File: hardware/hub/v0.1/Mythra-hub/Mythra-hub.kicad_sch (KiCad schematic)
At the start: 1 part, among them U1 TUSB8042A

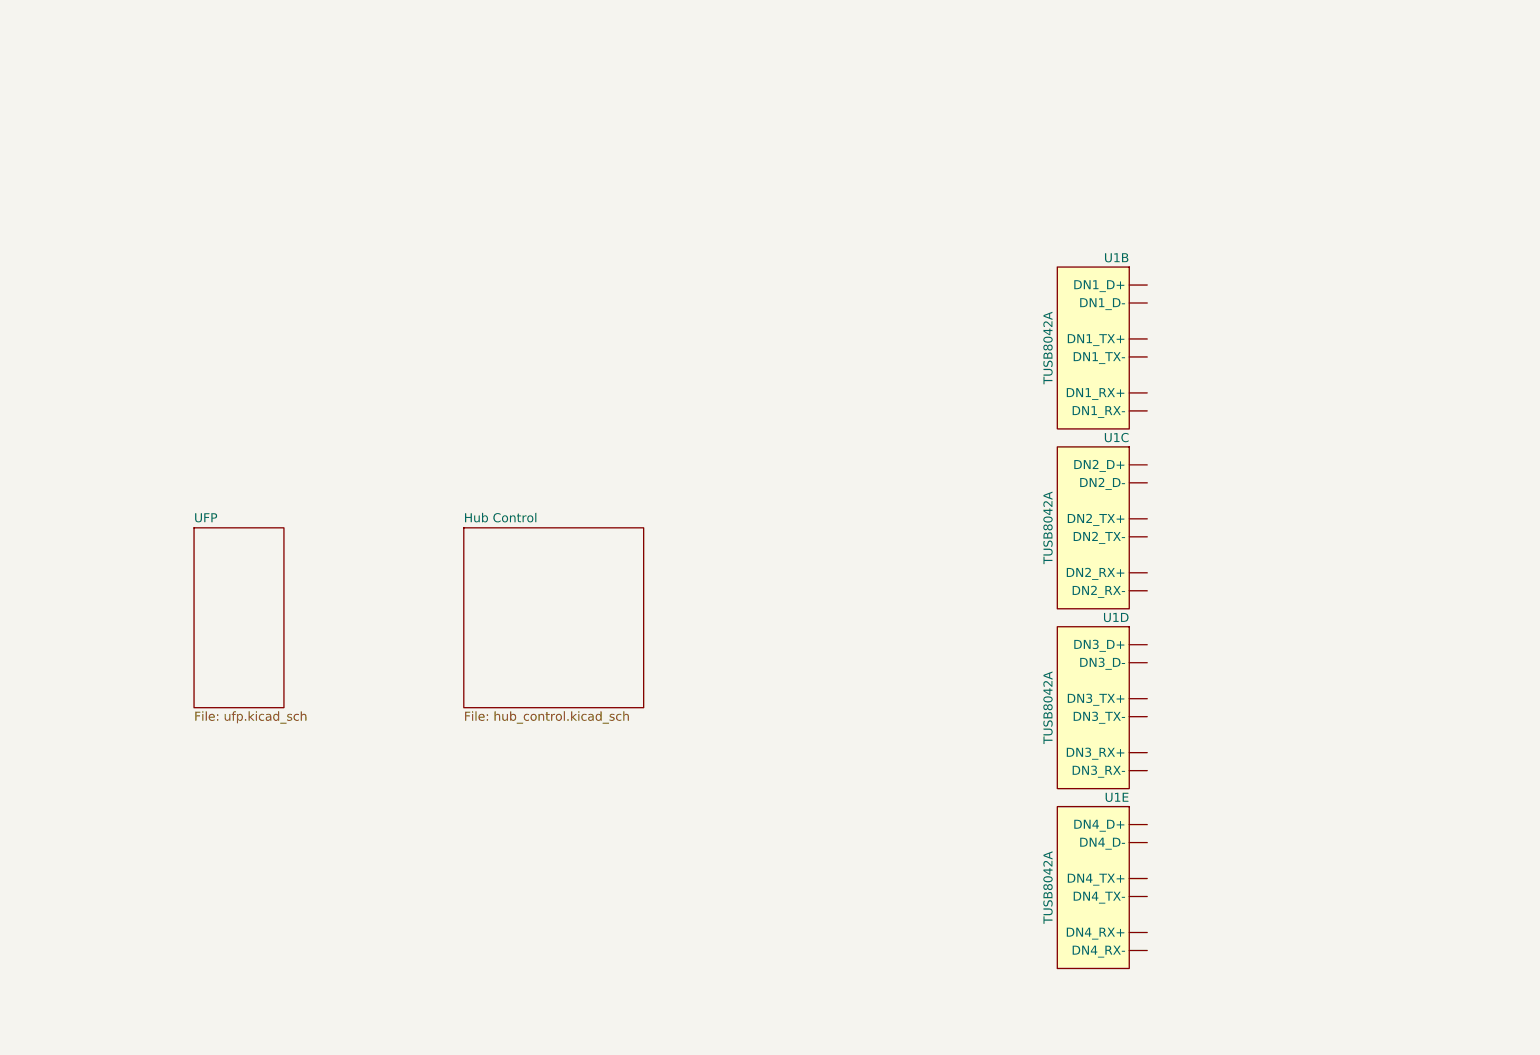
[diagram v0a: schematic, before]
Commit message: Re-jigged the hierachy and performed some cleanup
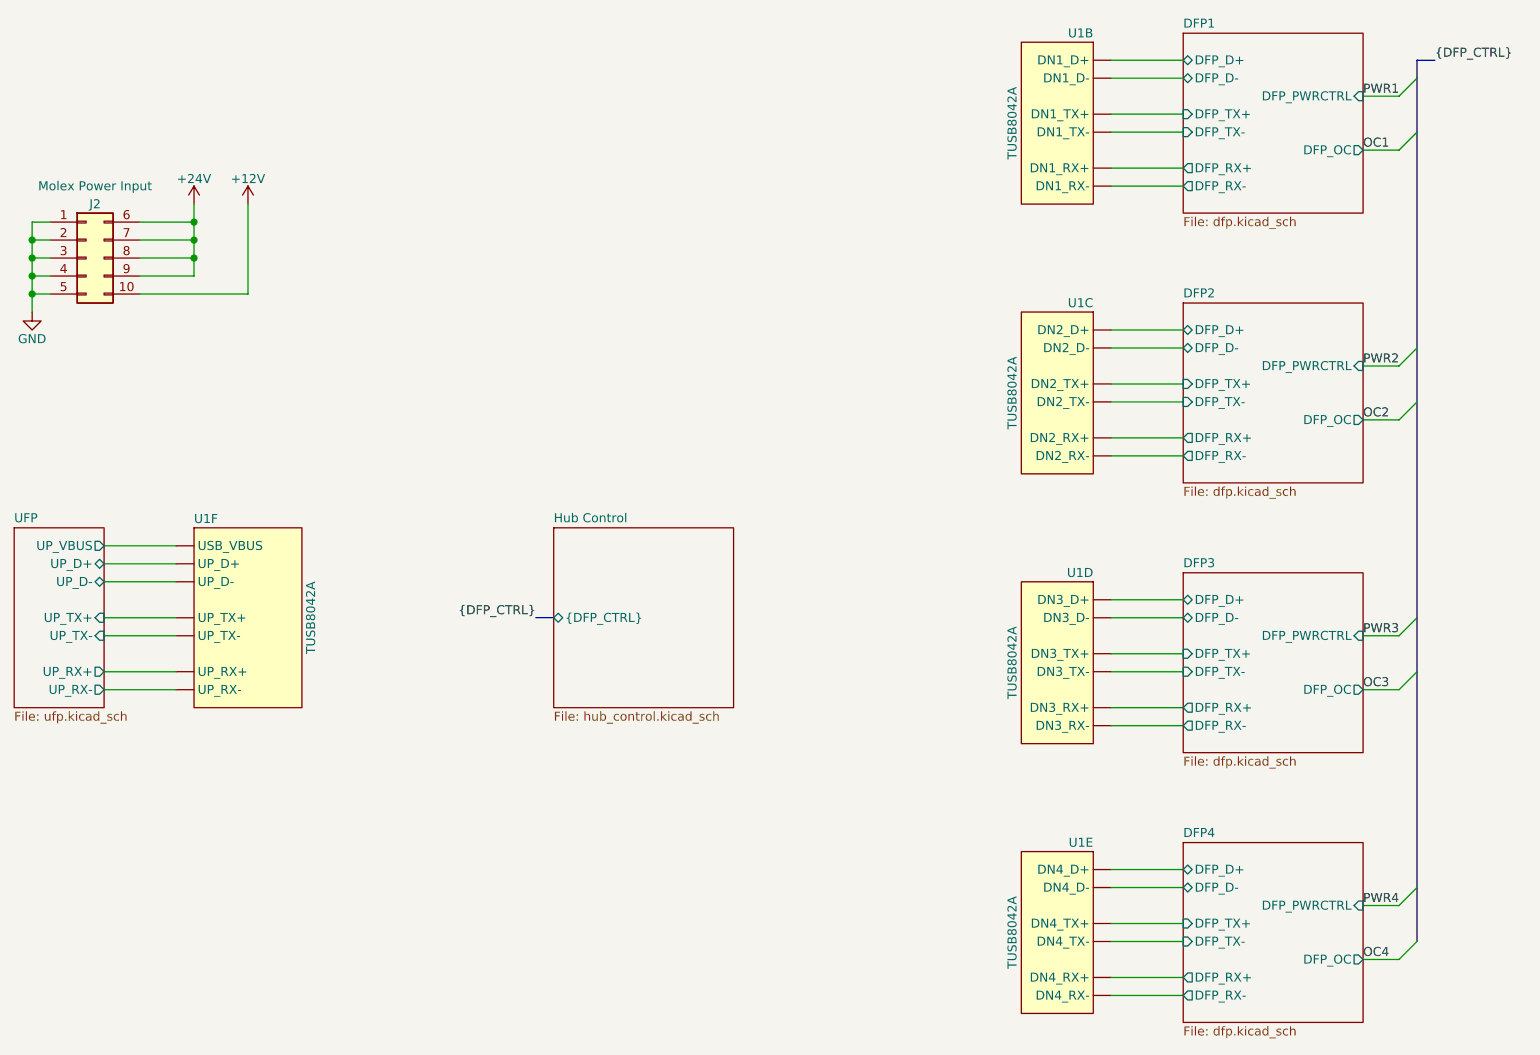
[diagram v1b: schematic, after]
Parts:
- added J2: Molex Power Input, rhais_connector-molex:39-30-1101, symbol Connector_Generic:Conn_02x05_Top_Bottom
- added unit 6 of U1
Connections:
- net DFP1/DFP_D+: now reaches U1.1 (DN1_D+)
- net DFP1/DFP_D-: now reaches U1.2 (DN1_D-)
- net DFP1/DFP_TX+: now reaches U1.3 (DN1_TX+)
- net DFP1/DFP_TX-: now reaches U1.4 (DN1_TX-)
- net DFP1/DFP_RX+: now reaches U1.6 (DN1_RX+)
- net DFP1/DFP_RX-: now reaches U1.7 (DN1_RX-)
- net DFP2/DFP_D-: now reaches U1.10 (DN2_D-)
- net DFP2/DFP_TX+: now reaches U1.11 (DN2_TX+)
- net DFP2/DFP_TX-: now reaches U1.12 (DN2_TX-)
- net DFP2/DFP_RX+: now reaches U1.14 (DN2_RX+)
- net DFP2/DFP_RX-: now reaches U1.15 (DN2_RX-)
- net DFP2/DFP_D+: now reaches U1.9 (DN2_D+)
- net DFP4/DFP_D+: now reaches U1.24 (DN4_D+)
- net DFP4/DFP_D-: now reaches U1.25 (DN4_D-)
- net DFP4/DFP_TX+: now reaches U1.26 (DN4_TX+)
- net DFP4/DFP_TX-: now reaches U1.27 (DN4_TX-)
- net DFP4/DFP_RX+: now reaches U1.29 (DN4_RX+)
- net DFP4/DFP_RX-: now reaches U1.30 (DN4_RX-)
- net DFP3/DFP_D+: now reaches U1.17 (DN3_D+)
- net DFP3/DFP_D-: now reaches U1.18 (DN3_D-)
- net DFP3/DFP_TX+: now reaches U1.19 (DN3_TX+)
- net DFP3/DFP_TX-: now reaches U1.20 (DN3_TX-)
- net DFP3/DFP_RX+: now reaches U1.22 (DN3_RX+)
- net DFP3/DFP_RX-: now reaches U1.23 (DN3_RX-)
- new net +12V: J2.10 (Pin_10)
- new net +24V: J2.6 (Pin_6), J2.7 (Pin_7), J2.8 (Pin_8), J2.9 (Pin_9)
- new net GND: J2.1 (Pin_1), J2.2 (Pin_2), J2.3 (Pin_3), J2.4 (Pin_4), J2.5 (Pin_5)
- new net UFP/UP_D+: U1.53 (UP_D+)
- new net UFP/UP_D-: U1.54 (UP_D-)
- new net UFP/UP_RX+: U1.58 (UP_RX+)
- new net UFP/UP_RX-: U1.59 (UP_RX-)
- new net UFP/UP_TX+: U1.55 (UP_TX+)
- new net UFP/UP_TX-: U1.56 (UP_TX-)
- new net UFP/UP_VBUS: U1.48 (USB_VBUS)
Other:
- added sheet DFP1 (dfp.kicad_sch)
- added sheet DFP2 (dfp.kicad_sch)
- added sheet DFP3 (dfp.kicad_sch)
- added sheet DFP4 (dfp.kicad_sch)
- sheet Hub Control ports: added {DFP_CTRL}; removed none
- sheet UFP ports: added UP_D+, UP_D-, UP_RX+, UP_RX-, UP_TX+, UP_TX-, UP_VBUS; removed none
- moved on the sheet: U1B, U1C, U1D, U1E

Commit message: Created the DC-DC supply for the hub's core 1.1V rail and added the DFP Type-C recepticals and their shield components
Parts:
- J2: MFR (none) -> Molex; MPN (none) -> 39-30-1101; OC_FARNELL (none) -> 3107197; URL_FARNELL (none) -> https://uk.farnell.com/molex/39-30-1101/connector-header-10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
